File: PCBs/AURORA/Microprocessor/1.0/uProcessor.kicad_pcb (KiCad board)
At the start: 2 copper layers, 85 x 55 mm, 63 parts, among them J1 Conn_01x03_Pin, J10 Conn_01x03_Pin, J11 Conn_01x02_Male, J12 Conn_01x04_Pin, J13 Conn_01x04_Pin, J14 Conn_01x02_Male, J15 Conn_01x05_Pin, J16 Conn_01x03_Pin, J17 Conn_01x02_Male, J18 Conn_01x04_Pin, J19 Conn_01x02_Male, J2 Conn_01x02_Male, J3 Conn_01x02_Male, J4 Conn_01x02_Male, J5 Conn_01x02_Male, J6 Conn_01x04_Pin, J7 Conn_01x02_Male, J8 Conn_01x04_Pin, Q1 BC817, Q2 BC817, SW1 TS-1187A-B-A-B, U1 ESP32-WROOM-32, U2 TCA9517DR, U3 TMP100

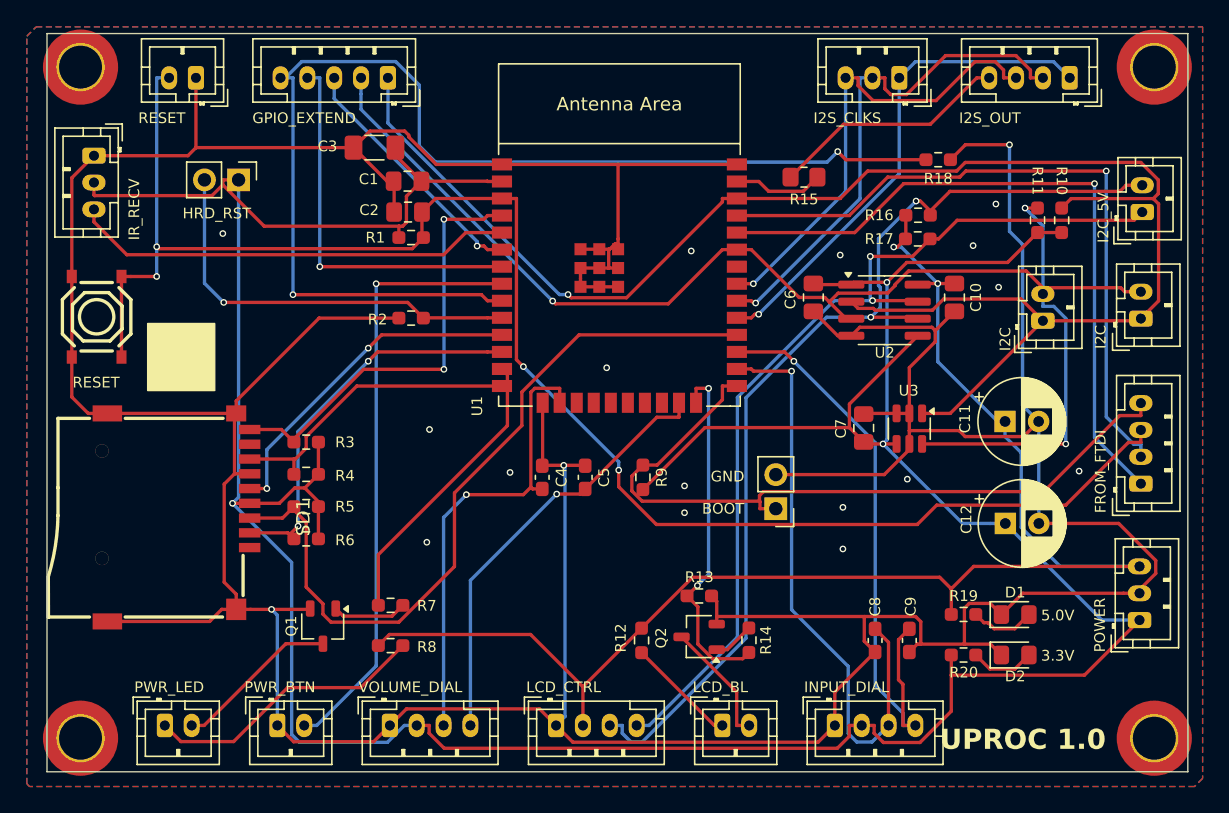
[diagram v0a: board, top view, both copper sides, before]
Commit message: Updates to amplifer
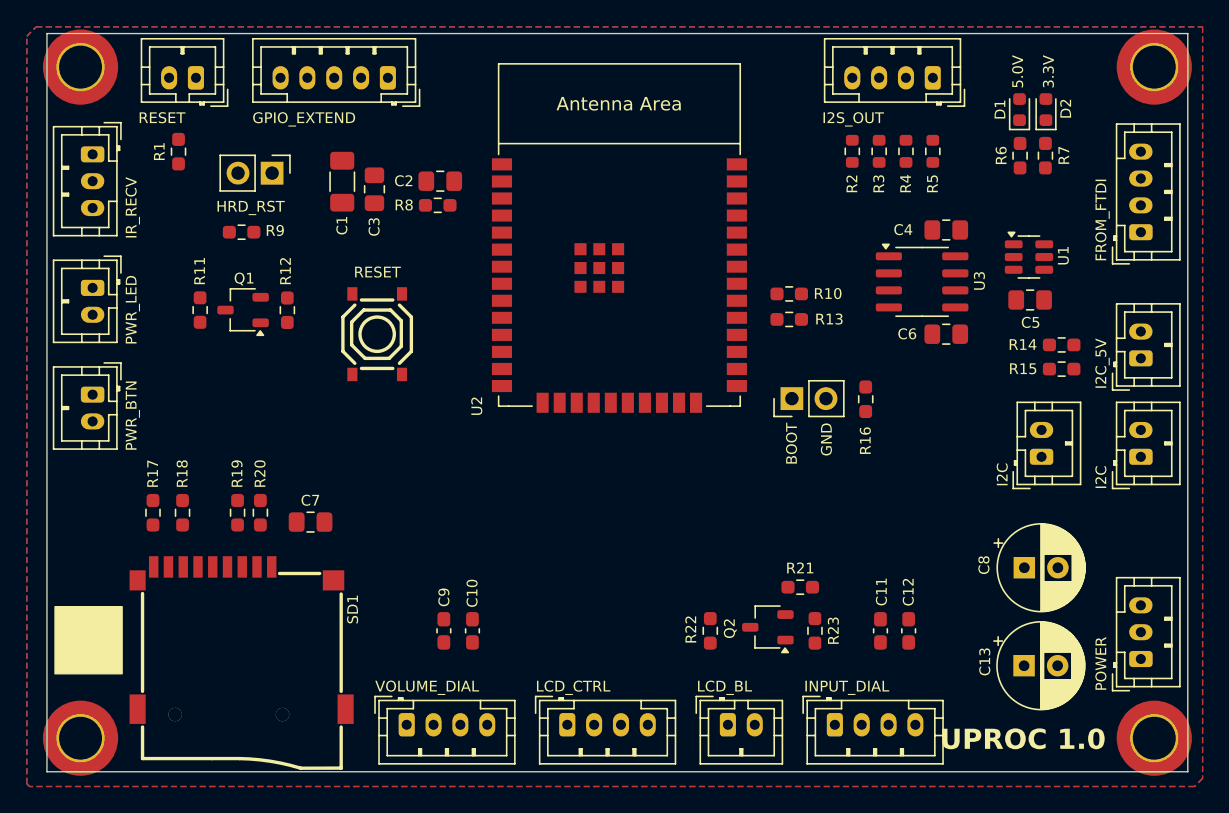
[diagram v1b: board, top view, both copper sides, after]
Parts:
- removed the J10 at (152.4, 66.3)
- added C7: 10N, Capacitor_SMD:C_0805_2012Metric_Pad1.18x1.45mm_HandSolder, F.Cu at (108.5, 99.4)
- added R3: 22R, Resistor_SMD:R_0603_1608Metric, F.Cu at (150.9, 71.8)
- added R4: 22R, Resistor_SMD:R_0603_1608Metric, F.Cu at (152.9, 71.8)
- added R5: 22R, Resistor_SMD:R_0603_1608Metric, F.Cu at (154.9, 71.8)
- D1: value ORANGE -> RED; footprint LED_SMD:LED_0805_2012Metric_Pad1.15x1.40mm_HandSolder -> LED_SMD:LED_0603_1608Metric
- D2: value YELLOW -> BLUE; footprint LED_SMD:LED_0805_2012Metric_Pad1.15x1.40mm_HandSolder -> LED_SMD:LED_0603_1608Metric
- R2: renamed from R15; footprint Resistor_SMD:R_0805_2012Metric_Pad1.20x1.40mm_HandSolder -> Resistor_SMD:R_0603_1608Metric
- R7: renamed from R20; value 430R -> 150R
- moved R1 56.6 mm to (98.7, 71.8), turned to 90 degrees
- moved D2 40.7 mm to (163.3, 68.7), turned to 90 degrees
- moved R7 37.7 mm to (163.3, 72.1), turned to 90 degrees
- moved D1 37.6 mm to (161.4, 68.7), turned to 90 degrees
- moved R6 34.4 mm to (161.4, 72.1), turned to 90 degrees
- moved J7 33.0 mm to (92.3, 82.0), turned to -90 degrees
- moved R11 28.7 mm to (100.3, 83.6), turned to -90 degrees
- moved J10 28.2 mm to (92.3, 89.9), turned to -90 degrees
- moved Q1 24.3 mm to (103.5, 83.6), turned to 180 degrees
- moved R12 23.3 mm to (106.8, 83.6), turned to -90 degrees
- moved R10 21.0 mm to (144.2, 82.4), turned to 180 degrees
- moved SW1 20.9 mm to (113.5, 85.4), turned to -90 degrees
- moved R13 19.9 mm to (144.2, 84.3), turned to 180 degrees
- moved J6 18.7 mm to (170.4, 77.8)
- moved R16 17.6 mm to (149.9, 90.2)
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- renumbered C3 to C1, C5 to C10, C8 to C11, C9 to C12, C12 to C13, C1 to C2, C2 to C3, C10 to C4, C7 to C5, C11 to C8, C4 to C9, H3 to H2, H2 to H3, J3 to J1, J5 to J10, J14 to J11, J17 to J12, J16 to J13, J6 to J14, J8 to J15, J11 to J16, J12 to J17, J15 to J2, J13 to J3, J1 to J4, J4 to J5, J18 to J6, J2 to J7, J19 to J8, J7 to J9, R18 to R1, R8 to R11, R7 to R12, R11 to R13, R16 to R14, R17 to R15, R9 to R16, R3 to R17, R4 to R18, R5 to R19, R6 to R20, R13 to R21, R12 to R22, R14 to R23, R19 to R6, R1 to R8, R2 to R9, U3 to U1, U1 to U2, U2 to U3
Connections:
- U2 pad 10: HARD_RESET -> POWER_LED
- U2 pad 11: SPI_CLK -> POWER_BUTTON
- U2 pad 12: SPI_CS -> SPI_MOSI
- U2 pad 13: POWER_LED -> SPI_CLK
- U2 pad 16: VOL_CH1 -> SPI_CS
- U2 pad 23: VOL_CH2 -> VOL_CH1
- U2 pad 24: BACKLIGHT -> VOL_CH2
- U2 pad 26: INPUT_CH1 -> BACKLIGHT
- U2 pad 27: INPUT_CH2 -> INPUT_CH1
- U2 pad 28: SPI_MOSI -> INPUT_CH2
- U2 pad 29: I2S_MCLK -> SDA
- U2 pad 30: I2S_BCLK -> SCL
- U2 pad 31: I2S_LRCLK -> Net-(U2-IO19)
- U2 pad 33: SDA -> Net-(U2-IO21)
- U2 pad 36: SCL -> Net-(U2-IO22)
- U2 pad 8: POWER_BUTTON -> GPIO_RESET
- U2 pad 9: GPIO_RESET -> HARD_RESET
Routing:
- net GND: track 385.4 -> 0.00 mm, vias 18 -> 0
- net 3V3: track 259.4 -> 0.00 mm, vias 3 -> 0
- net SCL: track 124.1 -> 0.00 mm, vias 1 -> 0
- net ENABLE: track 122.2 -> 0.00 mm, vias 4 -> 0
- net 5V: track 109.3 -> 0.00 mm, vias 2 -> 0
- net SDA: track 104.9 -> 0.00 mm, vias 3 -> 0
- net GPIO_RESET: track 87.4 -> 0.00 mm, vias 2 -> 0
- net SDA_5V: track 75.9 -> 0.00 mm, vias 2 -> 0
- net SCL_5V: track 69.5 -> 0.00 mm, vias 2 -> 0
- net SPI_MOSI: track 57.1 -> 0.00 mm
- net BOOT: track 56.1 -> 0.00 mm
- net RX: track 51.9 -> 0.00 mm, vias 1 -> 0
- net TX: track 51.6 -> 0.00 mm, vias 1 -> 0
- net POWER_BUTTON: track 45.0 -> 0.00 mm, vias 1 -> 0
- net INPUT_CH2: track 44.6 -> 0.00 mm, vias 1 -> 0
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- added copper zone on B.Cu, net (none)
- added copper zone on F.Cu, net (none)
- removed copper zone on B.Cu, net GND
- removed copper zone on F.Cu, net GND
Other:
- board text removed: "I2S_CLKS"
